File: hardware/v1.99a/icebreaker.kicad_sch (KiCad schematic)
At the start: 64 parts, among them J14 Jumper, J19 Jumper, J20 Flash, J21 PMOD, J22 PMOD, J23 PMOD, J26 5V AUX, J27 5V AUX, J28 CRESET, J3 Jumper, J4 Jumper, SW1 TACT, SW2 TACT, U2 3.3V, U3 1V2, U5 LY68L6400, U6 ICE40UP5K-SG48, U7 W25Q128JVxxM

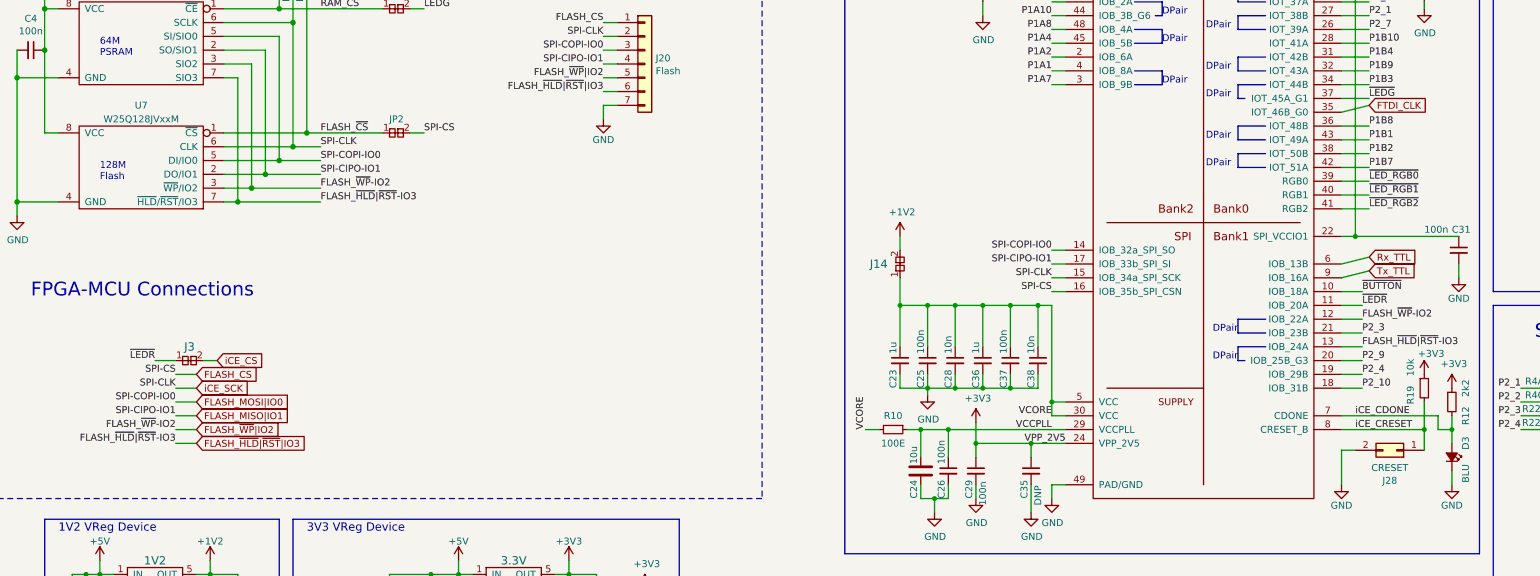
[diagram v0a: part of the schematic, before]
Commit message: v1.99a: Update
- Rename nets
- Add Debug UART channel to 10P SWD connector
- Add analog mux default on for iCE_CS/FLASH_CS
- Connect DONE/RESET
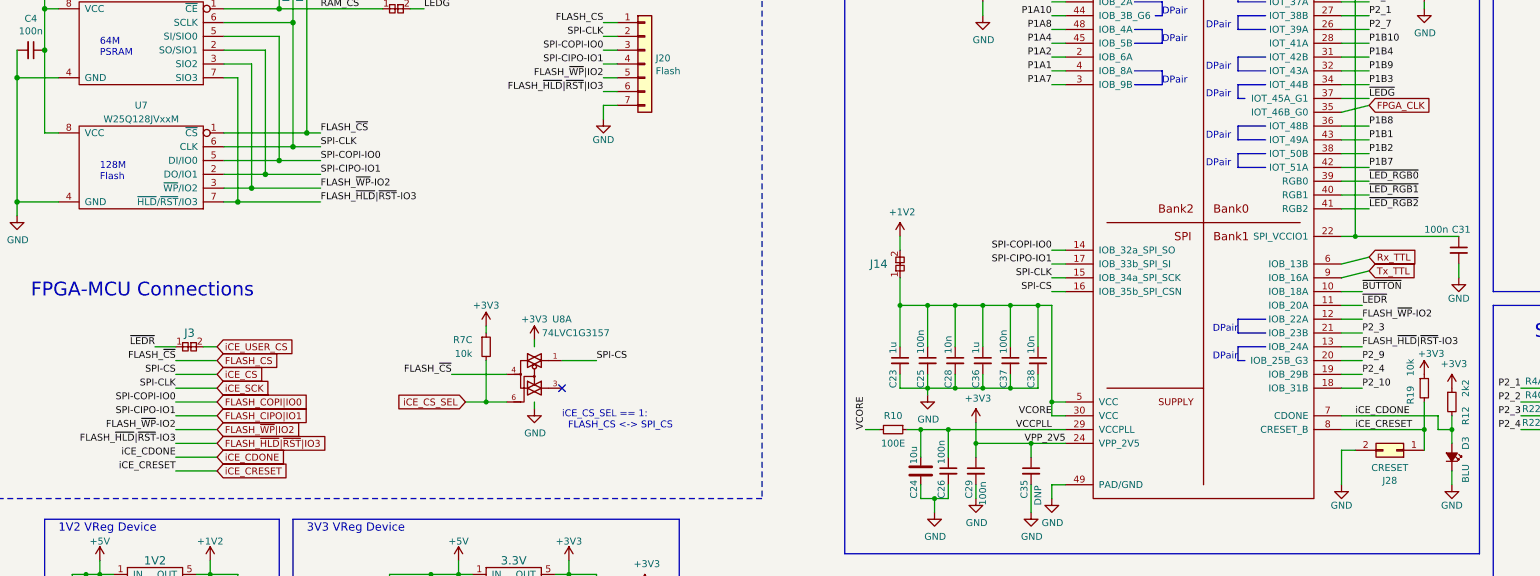
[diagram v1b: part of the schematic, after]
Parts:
- removed JP2: Flash_CS-SPI_CS, pkl_jumpers:J_NC_0402_15, symbol pkl_misc:pkl_jumper_nc
- added unit 3 of R7
- added U8: 74LVC1G3157, Package_TO_SOT_SMD:SOT-363_SC-70-6, symbol 74xGxx:74LVC1G3157
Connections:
- net FLASH_~{CS} is gone; now on net FLASH_CS: R7.8, U7.1 (~{CS})
- net +3V3: now also R7.5, U8.5 (VCC)
- net FLASH_CS: now also U8.4; no longer U6.16 (IOB_35b_SPI_CSN)
- net GND: now also U8.2 (GND)
- net iCE_CS: now also U6.16 (IOB_35b_SPI_CSN), U8.1; no longer J3.2
- net FLASH_MISO|IO1 renamed FLASH_CIPO|IO1
- net FLASH_MOSI|IO0 renamed FLASH_COPI|IO0
- net FTDI_CLK renamed FPGA_CLK
- new net iCE_CS_SEL: R7.6, U8.6
- new net iCE_USER_CS: J3.2
- no-connect marks 0 -> 1
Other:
- note added: "iCE_CS_SEL == 1: FLASH_CS <-> SPI_CS"
- moved on the sheet: J3

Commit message: Clean up the design.
- Remove R26.
- Connect BOOT0/1 to GND.
- Make schematic a single page.
- Rename labels to OSHWA recommendations.
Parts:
- added C1, C13, C14, C16, C17, C18, C19, C20: 0.1uF, Capacitor_SMD:C_0402_1005Metric, symbol Device:C
- added C10, C9: 18p, Capacitor_SMD:C_0402_1005Metric, symbol Device:C
- added C12: 4.7uF, Capacitor_SMD:C_0603_1608Metric, symbol Device:C
- added D6, D7: GRN, pkl_dipol:D_0603, symbol pkl_device:pkl_Led_Small
- added FB1: 220R, Inductor_SMD:L_0402_1005Metric, symbol Device:Ferrite_Bead
- added J1: USB_C_Receptacle_USB2.0, Connector_USB:USB_C_Receptacle_HRO_TYPE-C-31-M-12, symbol Connector:USB_C_Receptacle_USB2.0
- added J2: Conn_02x05_Odd_Even, Connector_PinHeader_1.27mm:PinHeader_2x05_P1.27mm_Vertical_SMD, symbol Connector_Generic:Conn_02x05_Odd_Even
- added R1, R8: 100k, Resistor_SMD:R_0402_1005Metric, symbol Device:R
- added R11, R9: 330E, pkl_dipol:R_0402, symbol pkl_device:pkl_R_Small
- added R2, R6: 5.1k, Resistor_SMD:R_0402_1005Metric, symbol Device:R
- added U1: TPD3S014, Package_TO_SOT_SMD:SOT-23-6, symbol Power_Protection:TPD3S014
- added U4: CH32V307VCT6, Package_QFP:LQFP-100_14x14mm_P0.5mm, symbol icebreaker_tmp:CH32V307VCT6
- added Y1: 24M, Crystal:Crystal_SMD_3225-4Pin_3.2x2.5mm, symbol Device:Crystal_GND24
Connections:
- net +3V3: now also C12.1, C14.1, C16.1, C17.1, C18.1, C19.1, C20.1, J2.1 (Pin_1), R8.1, U4.100 (VDD), U4.11 (VDD), U4.21 (VREF+), U4.22 (VDDA), U4.28 (VDD), U4.50 (VDD), U4.75 (VDD)
- net +5V: now also U1.4 (OUT)
- net FLASH_~{HLD}|~{RST}|IO3: now also U4.79 (PC11)
- net FLASH_~{WP}|IO2: now also U4.78 (PC10), U4.91 (PB5)
- net FPGA_CLK: now also U4.67 (PA8)
- net GND: now also C1.2, C10.2, C12.2, C13.2, C14.2, C16.2, C17.2, C18.2, C19.2, C20.2, C9.2, D6.C, D7.C, J1.A1 (GND), J1.A12 (GND), J1.B1 (GND), J1.B12 (GND), J2.3 (Pin_3), J2.5 (Pin_5), R1.2, R2.1, R6.1, U1.2 (GND), U4.10 (VSS), U4.19 (VSSA), U4.20 (VREF-), U4.27 (VSS), U4.37 (PB2/BOOT1), U4.49 (VSS), U4.74 (VSS), U4.94 (BOOT0), U4.99 (VSS), Y1.2, Y1.4
- net Rx_TTL: now also U4.95 (PB8), U4.98 (PE1)
- net Tx_TTL: now also U4.96 (PB9), U4.97 (PE0)
- net iCE_CDONE: now also U4.1 (PE2)
- net iCE_CRESET: now also U4.69 (PA10)
- net iCE_CS_SEL: now also U4.44 (PE13)
- net FLASH_CIPO|IO1 renamed SPI_POCI|IO1
- net SPI_POCI|IO1: now also U4.31 (PA6/ADC6), U4.54 (PB15), U4.66 (PC9/TXN)
- net FLASH_COPI|IO0 renamed SPI_PICO|IO0
- net SPI_PICO|IO0: now also U4.32 (PA7/ADC7), U4.53 (PB14), U4.65 (PC8/TXP)
- net FLASH_CS renamed FLASH_~{CS}
- net FLASH_~{CS}: now also U4.29 (PA4/ADC4/DAC0)
- net iCE_CS renamed iCE_~{CS}
- net iCE_~{CS}: now also U4.51 (PB12)
- net iCE_SCK renamed SPI_SCK
- net SPI_SCK: now also U4.30 (PA5/ADC5/DAC1), U4.52 (PB13), U4.80 (PC12)
- net iCE_USER_CS renamed iCE_USER_~{CS}
- net iCE_USER_~{CS}: now also U4.83 (PD2)
- new net: C9.1, U4.12 (OSC_IN), Y1.3
- new net: C10.1, U4.13 (OSC_OUT), Y1.1
- new net: J1.B5 (CC2), R6.2
- new net: FB1.1, J1.A4 (VBUS), J1.A9 (VBUS), J1.B4 (VBUS), J1.B9 (VBUS)
- new net: R9.1, U4.18 (PC3/ADC13)
- new net: D6.A, R9.2
- new net: R11.1, U4.17 (PC2/ADC12)
- new net: D7.A, R11.2
- new net: J1.A5 (CC1), R2.2
- new net DEBUG_RXD: J2.7 (Pin_7), U4.56 (PD9)
- new net DEBUG_TXD: J2.9 (Pin_9), U4.55 (PD8)
- new net NRST: J2.10 (Pin_10), R8.2, U4.14 (NRST)
- new net SHLD: C1.1, J1.S1 (SHIELD), R1.1
- new net SWCLK: J2.4 (Pin_4), U4.76 (PA14/SWCLK)
- new net SWDIO: J2.2 (Pin_2), U4.72 (PA13/SWDIO)
- new net USB_N: J1.A7 (D-), J1.B7 (D-), U1.5 (D1), U4.92 (PB6/USB2DM)
- new net USB_P: J1.A6 (D+), J1.B6 (D+), U1.6 (D2), U4.93 (PB7/USB2DP)
- new net VUSB: C13.1, FB1.2, U1.1 (EN), U1.3 (IN)
- no-connect marks 1 -> 54
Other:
- removed sheet usb-if
- note added: "(o) FLASH_~{WP}"
- note added: "(o) LED"
- note added: "(o) iCE_CRESET"
- note added: "MCO/TIM1_CH1"
- note added: "MCU -> Debug"
- note added: "MCU -> FLASH"
- note added: "MCU -> iCE40"
- note added: "MCU -> iCE40 (SDIO)"
- note added: "MCU <-> iCE40"
- note added: "MCU <-> iCE40 inverted"
- note added: "SDIO_CMD"
- note added: "SDIO_D0"
- note added: "SDIO_D1"
- note added: "SDIO_D2"
- note added: "SDIO_D3"
- note added: "SDIO_SCK"
- note added: "SPI1_CSN"
- note added: "SPI1_PICO"
- note added: "SPI1_POCI"
- note added: "SPI1_SCK"
- note added: "SPI2_PICO"
- note added: "SPI2_POCI"
- note added: "SPI2_SCK"
- note added: "SPI2_~{CS}"
- note added: "UART3_RX"
- note added: "UART3_TX"
- note added: "UART4_RX"
- note added: "UART4_TX"
- note added: "UART6_RX"
- note added: "UART6_TX"
- note added: "USBHS_DN"
- note added: "USBHS_DP"
- note added: "iCE_CDONE (i)"
- note added: "iCE_CS_SEL == 1: FLASH_CSN <-> SPI_CSN"
- note added: "iCE_~{CS}_SEL (o)"
- note removed: "FPGA-MCU Connections"
- note removed: "iCE_CS_SEL == 1: FLASH_CS <-> SPI_CS"
- moved on the sheet: C11, C15, C2, C3, C39, C4, C5, C8, D1, D2, D4, D5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
